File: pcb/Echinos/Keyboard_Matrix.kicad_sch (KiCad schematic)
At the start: 61 parts, among them J5 Joystick

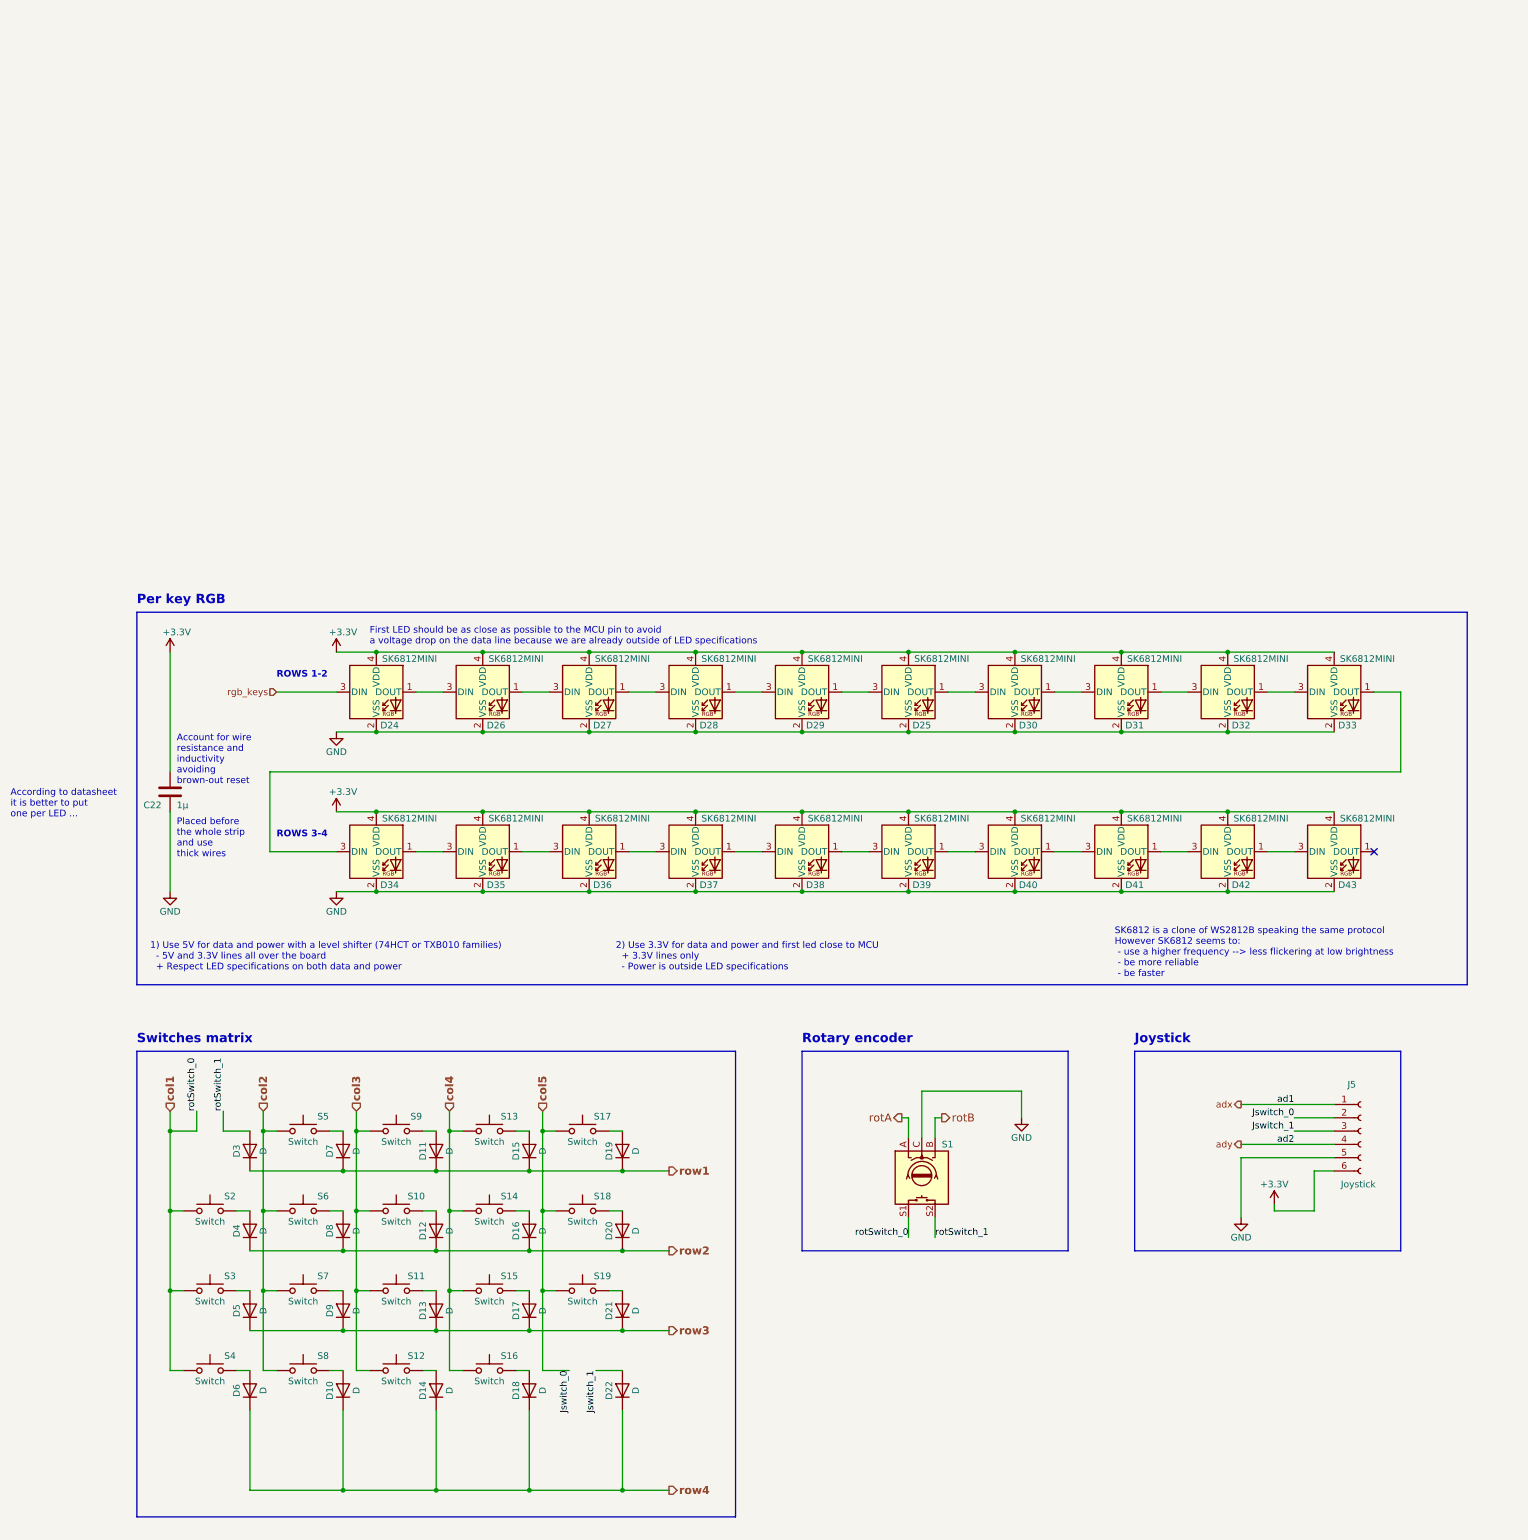
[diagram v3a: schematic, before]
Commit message: ✨ 🐛 ✅ [PCB] - Pass ERC test (exception to unconnected GPIO pins). Fix power symbol assignation to please Kicad. Fix duplicated line name (encoder / joystick) to please Kicad. Add trackball sensor connection documentation. Assign newly created footprints (encoder, joystick, switch).
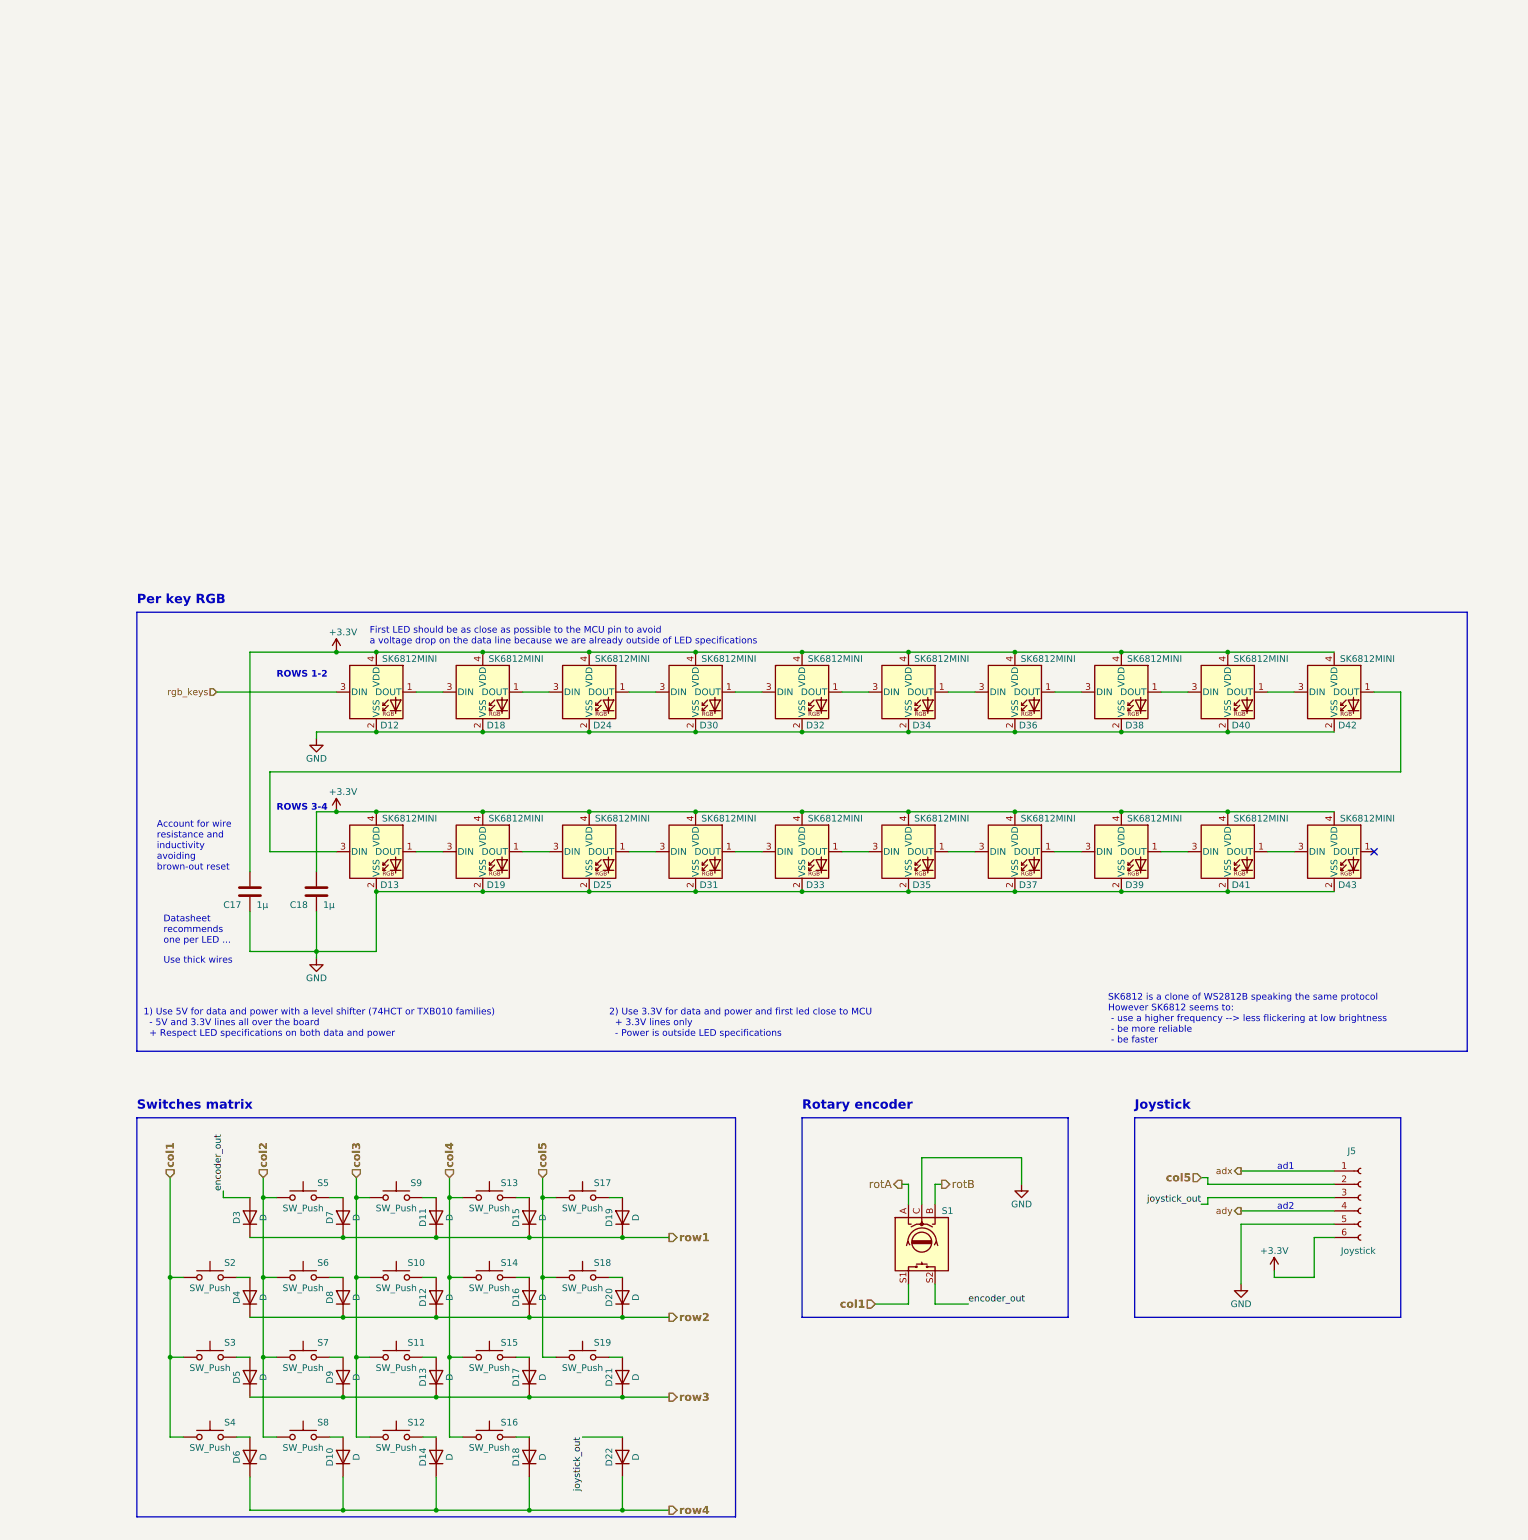
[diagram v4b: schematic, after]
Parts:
- removed C22: 1µ, Capacitor_SMD:C_0402_1005Metric, symbol Device:C
- added C17, C18: 1µ, Capacitor_SMD:C_0402_1005Metric, symbol Device:C
- J5: footprint Fuse:Fuse_0603_1608Metric_Pad1.05x0.95mm_HandSolder -> Echinos:Joystick_KSilver_JP19
- S1: footprint Echinos:PG1350-EVQWGD001 -> Echinos:SW_PG1350_1u_hotswap_EVQWGD001
- S10, S11, S12, S13, S14, S15, S16, S17, S18, S19, S2, S3, S4, S5, S6, S7, S8, S9: value Switch -> SW_Push; footprint Echinos:PG1350_hotswap -> Echinos:SW_PG1350_1u_hotswap
- renumbered D24 to D12, D34 to D13, D26 to D18, D35 to D19, D27 to D24, D36 to D25, D28 to D30, D37 to D31, D29 to D32, D38 to D33, D25 to D34, D39 to D35, D30 to D36, D40 to D37, D31 to D38, D41 to D39, D32 to D40, D42 to D41, D33 to D42
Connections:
- net GND: now also C17.2, C18.2
- net +3V3 renamed +3.3V
- net +3.3V: now also C17.1, C18.1
- net Jswitch_1 renamed joystick_out
- net rotSwitch_1 renamed encoder_out
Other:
- note added: "Datasheet recommends one per LED ..."
- note added: "Use thick wires"
- note added: "ad1"
- note added: "ad2"
- note removed: "According to datasheet it is better to put one per LED ..."
- note removed: "Placed before the whole strip and use thick wires"
- moved on the sheet: D10, D11, D12, D13, D14, D15, D16, D17, D18, D19, D20, D21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

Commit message: ✨ [PCB] - Complete schema and PCB for left halve. All connections are made. Optional encoder on the top outer key Optional joystick on either outer thumb or above middle thumb. Optional power LED (jumpers) SATA to connect both sides VIK compatible (except for 5.0V track) with enough space on the inner side to clip a VIK module Remaining MCU pins exposed with a 2.54mm spaced header All VIK modules are not yet placed / routed.
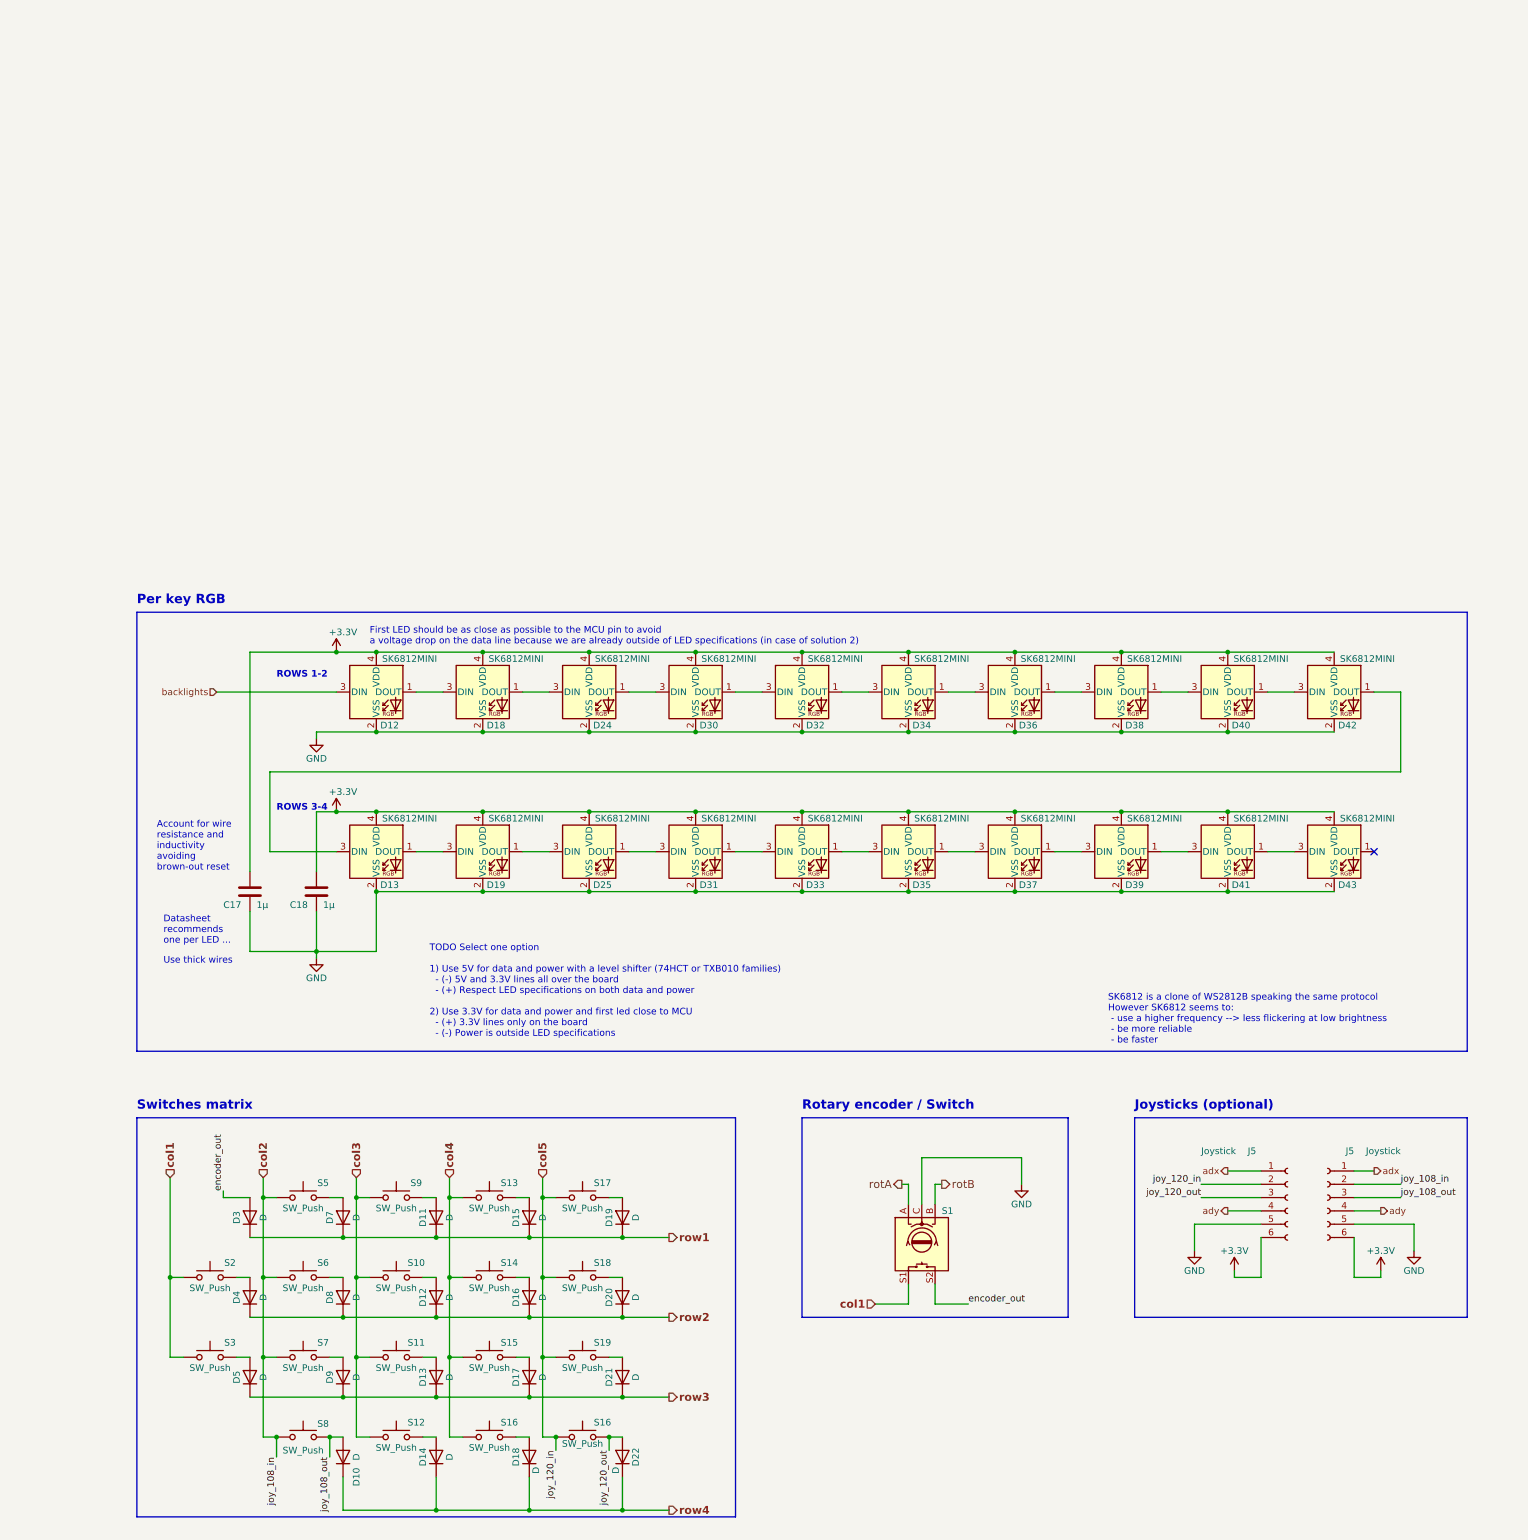
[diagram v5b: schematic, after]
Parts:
- removed D6: D, Echinos:D_SOD-123, symbol Device:D
- removed S4: SW_Push, Echinos:SW_PG1350_1u_hotswap, symbol Switch:SW_Push
- added J5: Joystick, Echinos:Joystick_KSilver_JP19, symbol Connector:Conn_01x06_Socket
- added S16: SW_Push, Echinos:SW_Choc_MX_KS33_1u_hotswap, symbol Switch:SW_Push
- D10, D11, D12, D13, D14, D15, D16, D17, D18, D19, D20, D21, D22, D3, D4, D5, D7, D8, D9: footprint Echinos:D_SOD-123 -> Echinos:D_SOD123
- S1: footprint Echinos:SW_PG1350_1u_hotswap_EVQWGD001 -> Echinos:SW_Choc_MX_KS33_1u_hotswap_EC12E
- S10, S11, S12, S13, S14, S15, S16, S17, S18, S19, S2, S3, S5, S6, S7, S8, S9: footprint Echinos:SW_PG1350_1u_hotswap -> Echinos:SW_Choc_MX_KS33_1u_hotswap
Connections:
- net +3.3V: now also J5.6 (Pin_6)
- net GND: now also J5.5 (Pin_5)
- net adx: now also J5.1 (Pin_1)
- net ady: now also J5.4 (Pin_4)
- net col2: now also J5.2 (Pin_2)
- net col5: now also S16.1
- net joy_108_out: now reaches D10.2 (A), S8.2
- net joy_108_out: now also J5.3 (Pin_3)
- net joystick_out renamed joy_120_out
- net joy_120_out: now also S16.2
- net rgb_keys renamed backlights
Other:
- note added: "First LED should be as close as possible to the MCU pin to avoid a voltage drop on the data line because we are already outside of LED specifications (in case of solution 2)"
- note added: "Joysticks (optional)"
- note added: "Rotary encoder / Switch"
- note added: "TODO Select one option 1) Use 5V for data and power with a level shifter (74HCT or TXB010 families) - (-) 5V and 3.3V lines all over the board - (+) Respect LED specifications on both data and power 2) Use 3.3V for data and power and first led close to MCU - (+) 3.3V lines only on the board - (-) Power is outside LED specifications"
- note removed: "1) Use 5V for data and power with a level shifter (74HCT or TXB010 families) - 5V and 3.3V lines all over the board + Respect LED specifications on both data and power"
- note removed: "2) Use 3.3V for data and power and first led close to MCU + 3.3V lines only - Power is outside LED specifications"
- note removed: "First LED should be as close as possible to the MCU pin to avoid a voltage drop on the data line because we are already outside of LED specifications"
- note removed: "Joystick"
- note removed: "Rotary encoder"
- note removed: "ad1"
- note removed: "ad2"
- moved on the sheet: J5
